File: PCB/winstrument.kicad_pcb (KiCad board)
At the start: 2 copper layers, 55 x 60 mm, 117 parts, among them J1 Conn_01x05_Pin, J2 Conn_01x03_Pin, J3 Conn_02x04_Odd_Even, J4 RS422, J5 Conn_01x08_Pin, J6 Conn_01x02_Pin, J7 ICSP, Q1 2N7002, Q2 2N7002, Q3 2N7002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

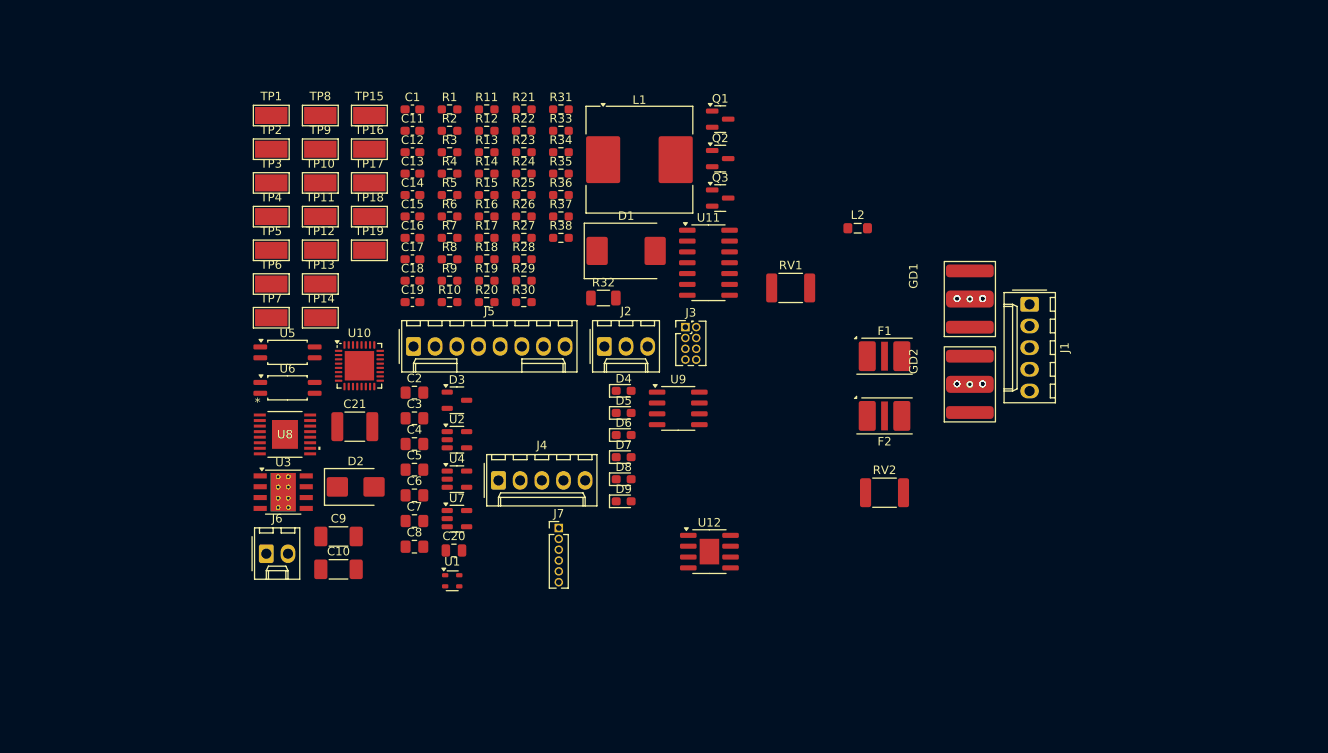
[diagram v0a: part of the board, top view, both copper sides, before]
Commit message: commit to catch up the repo to changes in PCB design
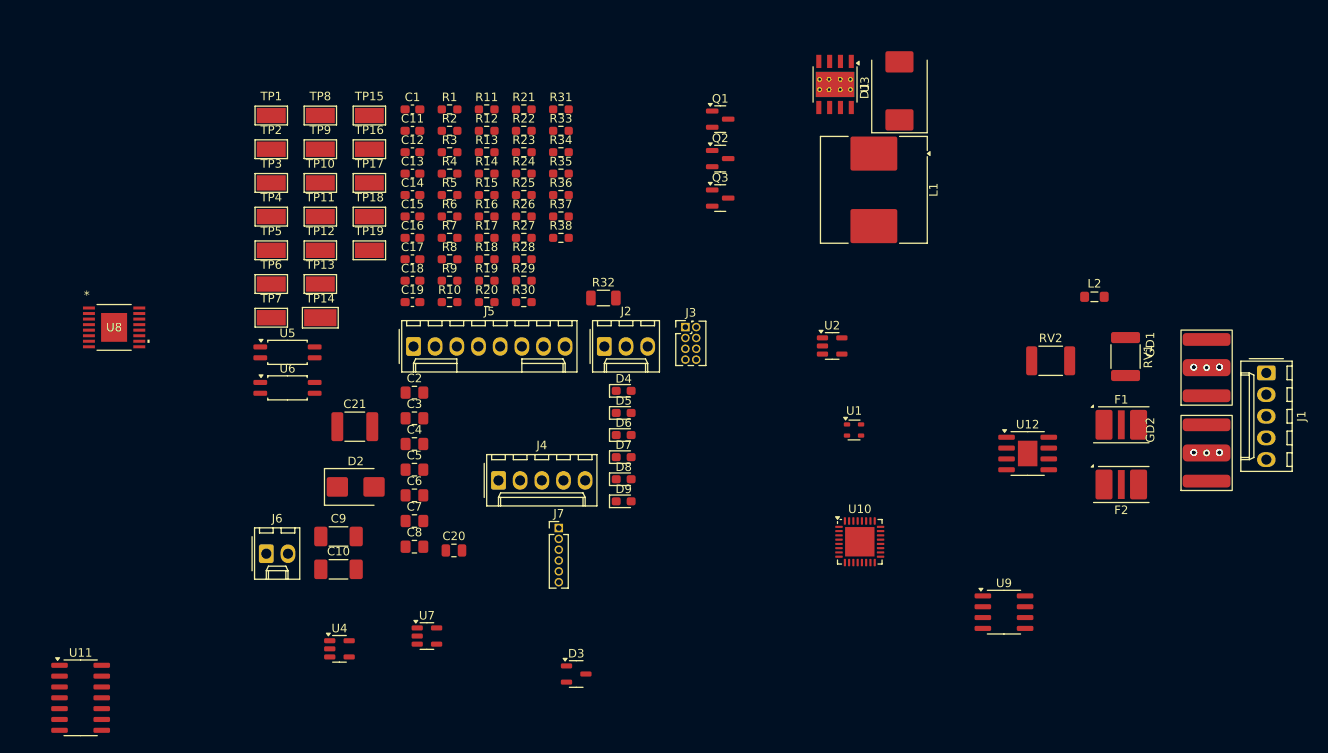
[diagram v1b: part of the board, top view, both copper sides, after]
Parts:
- TP1, TP10, TP11, TP12, TP13, TP15, TP16, TP17, TP18, TP19, TP2, TP3, TP4, TP5, TP6, TP7, TP8, TP9: footprint TestPoint:TestPoint_Keystone_5019_Minature -> TestPoint:TestPoint_Keystone_5015_Micro-Minature
- moved U11 89.5 mm to (100.8, 140.0)
- moved U3 80.4 mm to (189.2, 68.2), turned to -90 degrees
- moved U10 62.2 mm to (192.1, 121.8)
- moved U1 50.3 mm to (191.4, 108.7)
- moved U2 45.3 mm to (188.9, 98.8)
- moved U9 45.0 mm to (209.0, 130.0)
- moved RV1 40.1 mm to (223.2, 100.0), turned to -90 degrees
- moved U12 39.0 mm to (211.8, 111.4)
- moved D1 37.1 mm to (196.8, 68.9), turned to 90 degrees
- moved D3 35.0 mm to (158.9, 137.2)
- moved F1 28.9 mm to (222.8, 108.0)
- moved F2 28.9 mm to (222.8, 115.0)
- moved GD1 28.9 mm to (232.8, 104.6)
- moved GD2 28.9 mm to (232.8, 114.6)
- moved L2 28.9 mm to (219.6, 93.0)
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
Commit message: modified schematics to replace parts and redesign serial interfaces.  Replaced general purpose opamps with adjustable gain instrumentation amplifiers that are more appropriate.
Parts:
- added J5: Conn_01x09_Pin, Connector_Molex:Molex_KK-254_AE-6410-09A_1x09_P2.54mm_Vertical, F.Cu at (1.79, 3.44)
- added L3: MSD1278-105, CoilcraftPCB:MSD1278 SERIES, F.Cu at (216.0, 98.7)
- moved C9 87.7 mm to (206.5, 76.5)
- moved C10 87.6 mm to (206.4, 80.5)
- moved D2 73.4 mm to (205.0, 101.0), turned to -90 degrees
- moved R4 68.2 mm to (211.6, 69.0)
- moved J3 67.9 mm to (104.2, 88.2)
- moved R3 63.0 mm to (206.6, 69.0)
- moved C2 52.8 mm to (183.5, 74.5)
- moved C3 52.5 mm to (183.5, 78.0)
- moved C1 52.3 mm to (191.1, 61.5)
- moved C4 52.2 mm to (183.5, 81.5)
- moved L2 14.0 mm to (206.2, 89.0)
- moved RV2 13.1 mm to (227.0, 104.5), turned to 90 degrees
- moved RV1 4.27 mm to (227.0, 98.0)
- moved F1 3.69 mm to (225.5, 110.5)
- moved F2 2.79 mm to (225.5, 115.5)
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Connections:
- R13 pad 1: /V_LOAD -> +3V3
- R9 pad 1: /V_LOAD -> +3V3
- U10 pad 13: /STAT_3 -> /CAN_FAULT
